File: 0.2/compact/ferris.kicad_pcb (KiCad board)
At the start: 2 copper layers, 208.8 x 86.8 mm, 109 parts, among them J1 TYPE-C-31-M-12, K0_0 KEYSW, K0_1 KEYSW, K0_2 KEYSW, K0_3 KEYSW, K0_4 KEYSW, K0_5 KEYSW, K0_6 KEYSW, K0_7 KEYSW, K0_8 KEYSW, K0_9 KEYSW, K1_0 KEYSW, K1_1 KEYSW, K1_2 KEYSW, K1_3 KEYSW, K1_4 KEYSW, K1_5 KEYSW, K1_6 KEYSW, K1_7 KEYSW, K1_8 KEYSW, K1_9 KEYSW, K2_0 KEYSW, K2_1 KEYSW, K2_2 KEYSW, K2_3 KEYSW, K2_4 KEYSW, K2_5 KEYSW, K2_6 KEYSW, K2_7 KEYSW, K2_8 KEYSW, K2_9 KEYSW, K3_3 KEYSW, K3_4 KEYSW, K3_5 KEYSW, K3_6 KEYSW, Q1 PDTC123JT,215, SW1 B3U-1000P, U1 STM32F072CBT6, U2 MCP23017-E/SO, U3 MCP1700T-3302E/TT, U4 SRV05-4

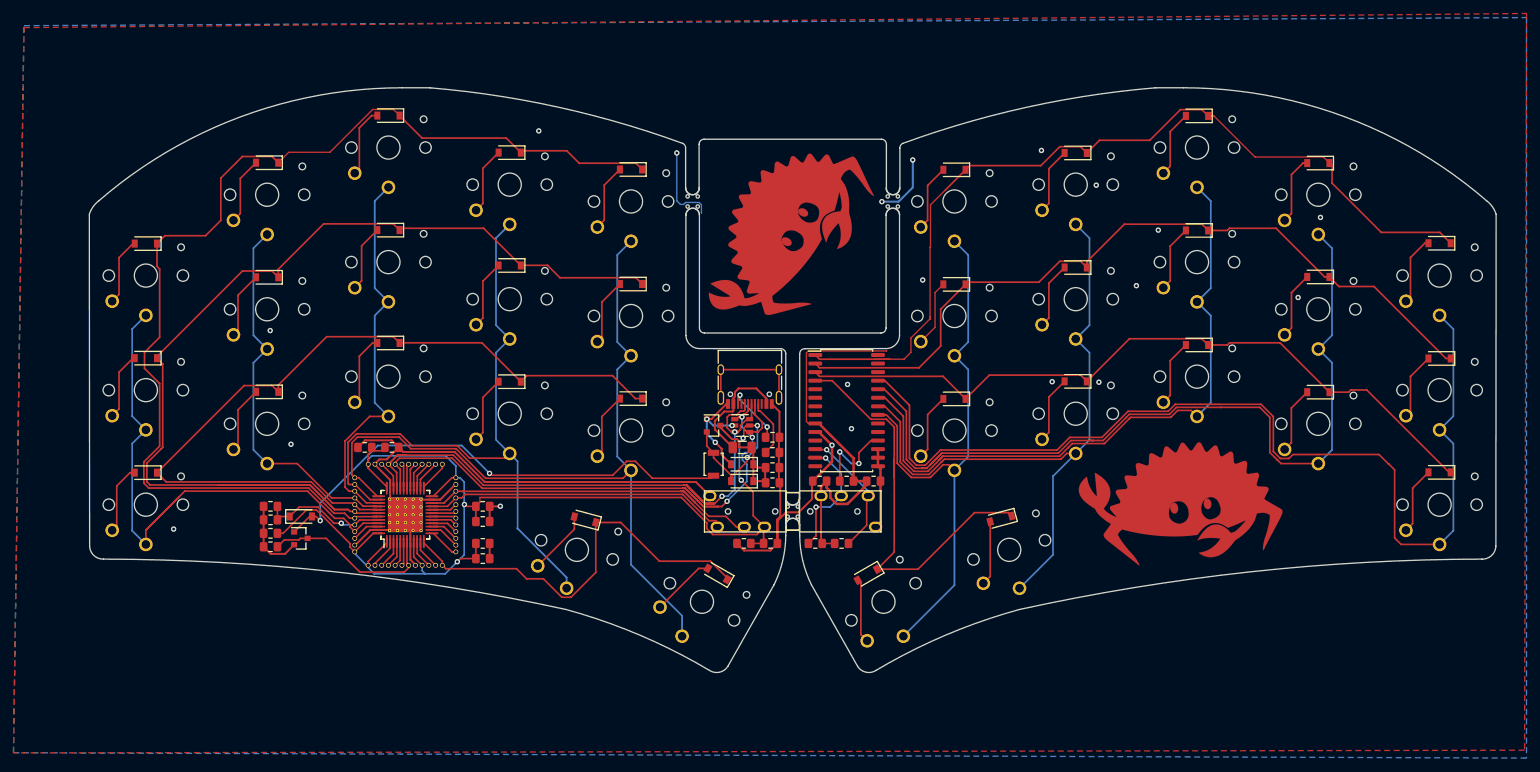
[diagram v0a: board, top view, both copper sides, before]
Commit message: Reroute traces and remove middle square
Traces were too close to drilling holes causing issue with JLCPCB,
The middle information square is pretty but counts as its own
design, increasing the price of the PCB by 1.5x.
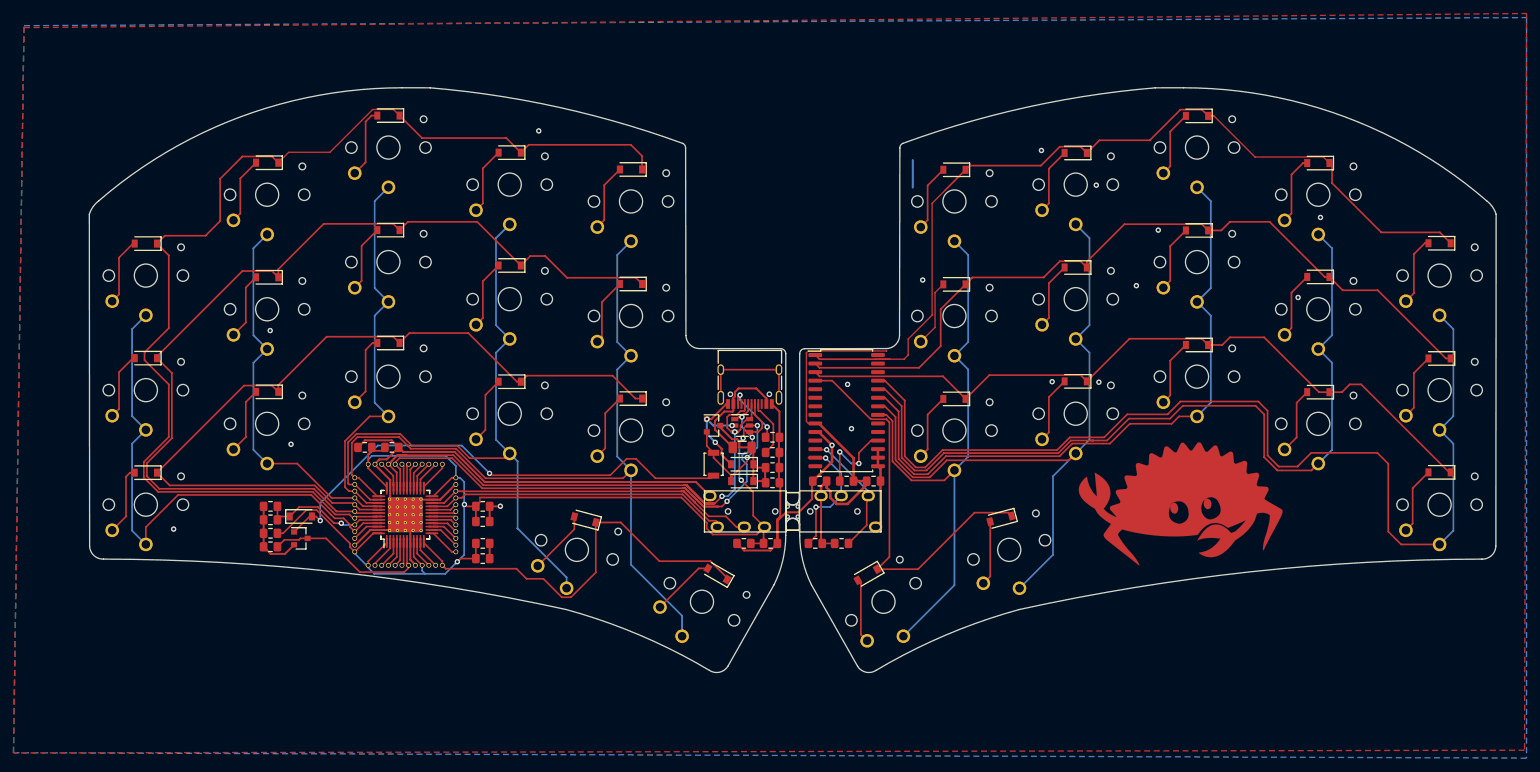
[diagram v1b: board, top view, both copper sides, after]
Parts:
- removed the G*** at (117.1, 34.8)
- removed the mouse-bite-2mm-slot at (132.8, 30.0)
- removed the mouse-bite-2mm-slot at (103.2, 30.0)
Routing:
- net /row0,1: track 163.1 -> 144.5 mm
- net GND: track 214.9 -> 197.0 mm, vias 23 -> 20
- net /col0: track 86.4 -> 79.2 mm
- net /row0,0: track 164.2 -> 167.8 mm
- net /row1,3: track 63.3 -> 60.0 mm
- net /col9: track 152.3 -> 155.2 mm
- net /row1,2: track 109.6 -> 111.0 mm
- net /row0,2: track 120.9 -> 122.1 mm
- net /col7: track 98.2 -> 97.1 mm
- net /row1,1: track 116.8 -> 117.6 mm
- net /col8: track 125.3 -> 124.7 mm
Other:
- outline, holes or cut-outs redrawn
- board text added: "by @pierrec83 modified by @SanderJSA illustrations from @whoisaldeka"
- board text removed: "Ferris Compact - v0.2.1 by @pierrec83 Minimalism shall prevail :D * Split, 34 Keys * Kailh Choc footprints: pg1350 * Choc spacing: 17x18mm * Microcontroller: STM32FO72 * IO Expander: MCP23017 * USB C * All MCU pins are broken out * Nothing frivolous Fully open source design: github.com/pierrechevalier83/ferris"
- board text removed: "by @pierrec83 illustrations from @whoisaldeka"
